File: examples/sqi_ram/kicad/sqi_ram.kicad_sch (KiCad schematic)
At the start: 19 parts, among them U1 GAL16V8 seq, U2 GAL16V8 sio, U3 74AC138, U4 74AC244, U5 74AC244, U6 74AC574, U7 23LC512, X1 32MHz

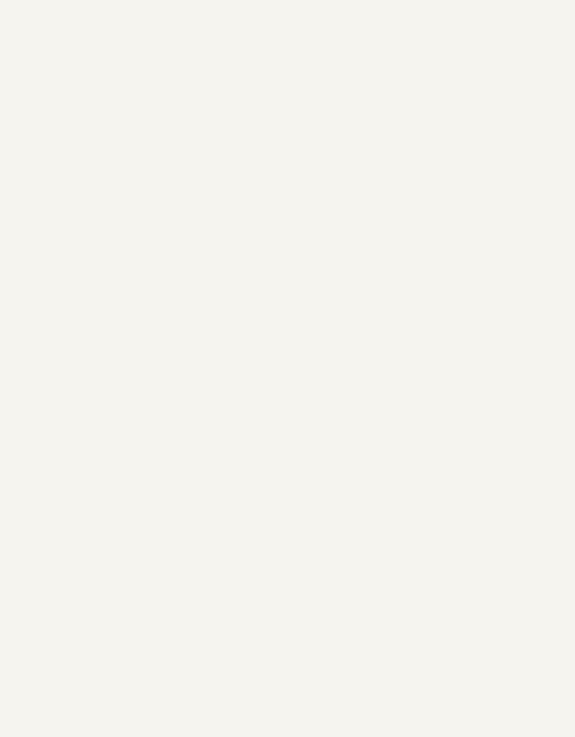
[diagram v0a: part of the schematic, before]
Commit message: Add a PCB for the SQI RAM interface
make_pcb.py places the schematic's footprints on a 95 x 72 mm two-layer
board, with a 2x16 header to the 8052 board, routes it with Freerouting
(neck-down off, so tracks keep their net class widths) and adds ground
pours. KiCad's DRC finds no violations and no unconnected pads, and every
pad's net matches the schematic netlist. Gerbers and drill files are in
sqi_ram-gerbers.zip.

Co-Authored-By: Claude Opus 5.5 <noreply@anthropic.com>
Claude-Session: https://claude.ai/code/session_018pPg39GKDWtHXfSGwKPAqj
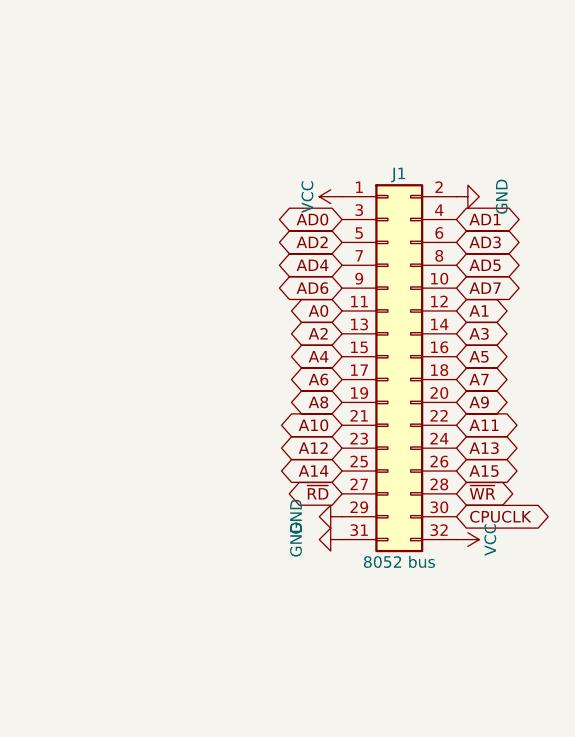
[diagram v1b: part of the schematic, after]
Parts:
- added J1: 8052 bus, Connector_PinHeader_2.54mm:PinHeader_2x16_P2.54mm_Vertical, symbol Connector_Generic:Conn_02x16_Odd_Even
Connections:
- net A0: now also J1.11 (Pin_11)
- net A1: now also J1.12 (Pin_12)
- net A10: now also J1.21 (Pin_21)
- net A11: now also J1.22 (Pin_22)
- net A12: now also J1.23 (Pin_23)
- net A13: now also J1.24 (Pin_24)
- net A14: now also J1.25 (Pin_25)
- net A15: now also J1.26 (Pin_26)
- net A2: now also J1.13 (Pin_13)
- net A3: now also J1.14 (Pin_14)
- net A4: now also J1.15 (Pin_15)
- net A5: now also J1.16 (Pin_16)
- net A6: now also J1.17 (Pin_17)
- net A7: now also J1.18 (Pin_18)
- net A8: now also J1.19 (Pin_19)
- net A9: now also J1.20 (Pin_20)
- net AD0: now also J1.3 (Pin_3)
- net AD1: now also J1.4 (Pin_4)
- net AD2: now also J1.5 (Pin_5)
- net AD3: now also J1.6 (Pin_6)
- net AD4: now also J1.7 (Pin_7)
- net AD5: now also J1.8 (Pin_8)
- net AD6: now also J1.9 (Pin_9)
- net AD7: now also J1.10 (Pin_10)
- net CPUCLK: now also J1.30 (Pin_30)
- net GND: now also J1.2 (Pin_2), J1.29 (Pin_29), J1.31 (Pin_31)
- net VCC: now also J1.1 (Pin_1), J1.32 (Pin_32)
- net ~{RD}: now also J1.27 (Pin_27)
- net ~{WR}: now also J1.28 (Pin_28)
